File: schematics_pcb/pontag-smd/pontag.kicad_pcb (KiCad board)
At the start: 2 copper layers, 31 parts, among them J1 External 5V, J2 External 12V, J3 RS232 Port, J4 PS/2 Mouse, J5 AVR-ISP-6, J7 Extra, SW1 Reset, U1 LP2985-5.0, U3 ATmega8A-AU, U4 MAX232A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

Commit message: Update schematics and PCB
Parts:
- moved D5 120.9 mm to (72.4, 132.1), turned to 90 degrees
- moved R2 108.3 mm to (72.4, 138.4), turned to 270 degrees
- moved J7 97.1 mm to (95.2, 138.4), turned to 180 degrees
- moved JP1 75.6 mm to (115.6, 100.3)
- moved J5 64.8 mm to (95.2, 114.3)
- moved U4 39.9 mm to (83.8, 119.4)
- moved SW1 30.5 mm to (67.3, 134.6), turned to 90 degrees
- moved J4 15.3 mm to (85.1, 134.6), turned to 0 degrees
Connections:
- net Net-(C12-Pad1) renamed /REG_5V

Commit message: Changed some connectors
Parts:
- J5: value AVR-ISP-6 -> ISP; footprint Connector_PinHeader_2.54mm:PinHeader_2x03_P2.54mm_Vertical -> Connector_PinHeader_2.54mm:PinHeader_1x06_P2.54mm_Vertical
- J7: footprint Connector_PinSocket_2.54mm:PinSocket_2x06_P2.54mm_Vertical -> Connector_PinSocket_2.54mm:PinSocket_2x03_P2.54mm_Vertical
- moved J5 25.0 mm to (105.4, 137.2)
- moved J7 17.4 mm to (112.6, 137.2), turned to 0 degrees
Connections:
- SW1 pad 1: GND -> /RESET
- SW1 pad 2: /RESET -> GND
- U3 pad 26: Net-(J7-Pad7) -> (no net)
- U3 pad 27: Net-(J7-Pad9) -> (no net)
- U3 pad 28: Net-(J7-Pad11) -> (no net)

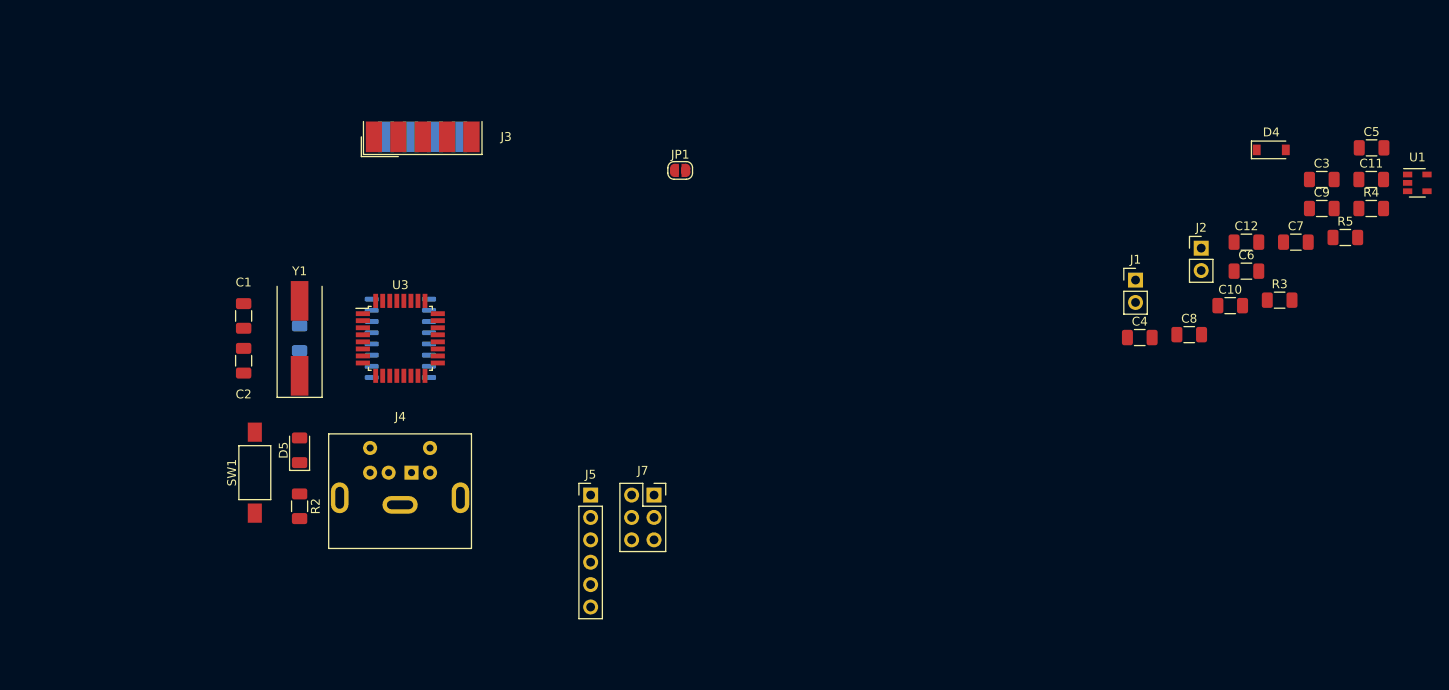
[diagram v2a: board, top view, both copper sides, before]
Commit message: Organize some components
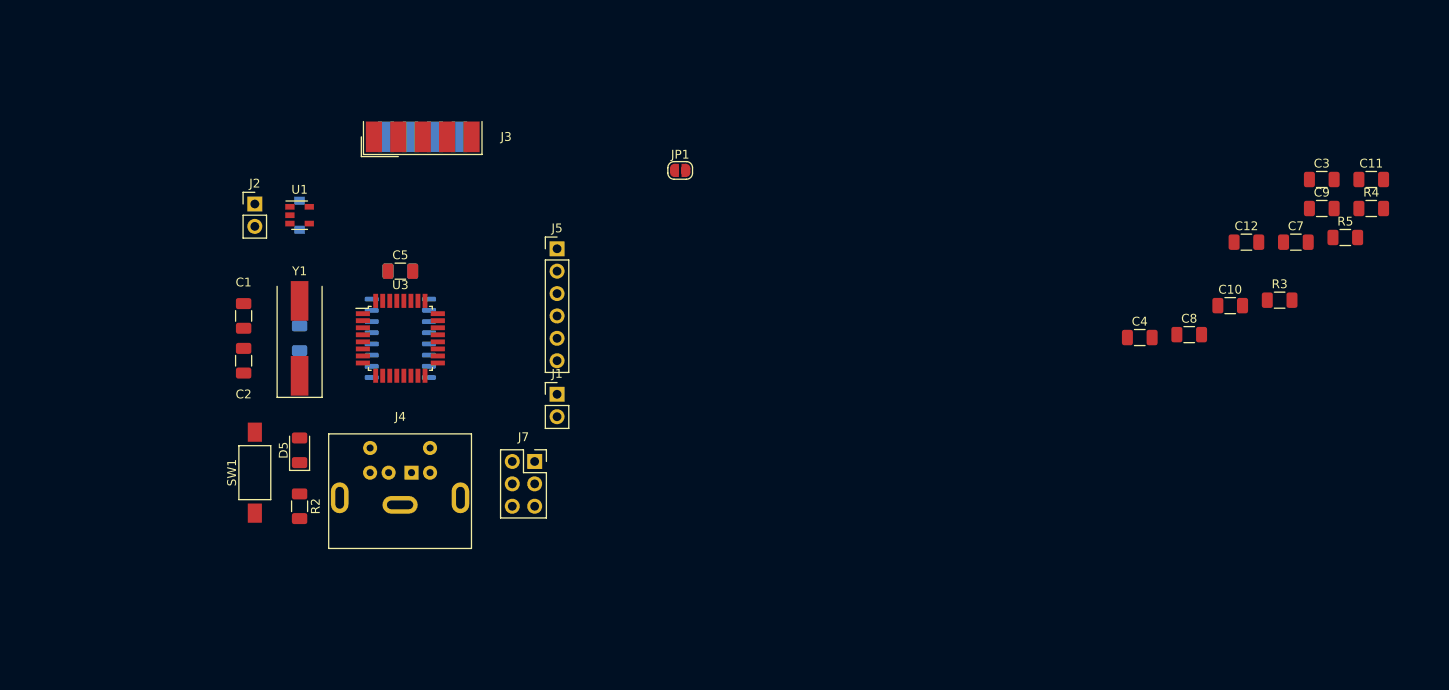
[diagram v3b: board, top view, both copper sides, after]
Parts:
- C6, D4: moved to B.Cu
- moved U1 126.9 mm to (72.4, 105.4)
- moved C5 111.1 mm to (83.8, 111.8)
- moved D4 110.5 mm to (72.4, 105.4), turned to 90 degrees
- moved J2 107.5 mm to (67.3, 104.1)
- moved C6 96.0 mm to (83.8, 111.8)
- moved J1 66.9 mm to (101.6, 125.7)
- moved J5 28.2 mm to (101.6, 109.2)
- moved J7 14.1 mm to (99.1, 133.3)

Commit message: Go on with board routing
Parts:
- C10, C11, C3, C7, C8, C9, R2, R3, R4, R5: moved to B.Cu
- J5: value ISP -> AVR-ISP-6; footprint Connector_PinHeader_2.54mm:PinHeader_1x06_P2.54mm_Vertical -> Connector_PinHeader_2.54mm:PinHeader_2x03_P2.54mm_Vertical
- moved R5 126.3 mm to (67.3, 133.3), turned to 270 degrees
- moved C3 116.2 mm to (72.4, 108.0)
- moved C11 115.5 mm to (78.7, 109.2)
- moved C9 111.3 mm to (77.5, 114.3), turned to 90 degrees
- moved R3 110.0 mm to (74.9, 132.1), turned to 90 degrees
- moved C12 107.4 mm to (72.4, 108.0), turned to 180 degrees
- moved R4 107.4 mm to (90.2, 132.1), turned to 270 degrees
- moved C7 106.8 mm to (78.7, 104.1), turned to 180 degrees
- moved C4 101.0 mm to (67.3, 108.0)
- moved C8 95.9 mm to (77.5, 120.7), turned to 90 degrees
- moved C10 95.8 mm to (82.5, 124.5)
- moved JP1 37.0 mm to (78.7, 104.1)
- moved R2 24.3 mm to (96.5, 135.9)
- moved D5 24.2 mm to (96.5, 133.3)
- moved J1 14.8 mm to (94.0, 113.0), turned to 90 degrees
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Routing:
- net /XTAL1: track 0.00 -> 10.0 mm
- net /XTAL2: track 0.00 -> 6.51 mm
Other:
- board outline added: 36.8 x 44.5 mm

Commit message: Updates on SMD PCB
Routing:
- net GND: track 0.00 -> 210.0 mm
- net VCC: track 0.00 -> 141.2 mm, vias 0 -> 2
- net /RESET: track 0.00 -> 100.7 mm, vias 0 -> 1
- net /MISO: track 0.00 -> 50.4 mm, vias 0 -> 1
- net /MOSI: track 0.00 -> 48.9 mm
- net /SCK: track 0.00 -> 43.3 mm
- net /RS232-RTS: track 0.00 -> 41.4 mm
- net /PS2-CLOCK: track 0.00 -> 29.9 mm, vias 0 -> 1
- net /PS2-DATA: track 0.00 -> 25.8 mm, vias 0 -> 1
- net /RS232-RX: track 0.00 -> 15.6 mm, vias 0 -> 1
- net Net-(C4-Pad1): track 0.00 -> 14.4 mm
- net /RS232-TX: track 0.00 -> 13.6 mm, vias 0 -> 1
- net +12V: track 0.00 -> 12.4 mm, vias 0 -> 1
- net /TTL-CTS: track 0.00 -> 12.0 mm, vias 0 -> 1
- net Net-(J7-Pad1): track 0.00 -> 11.9 mm
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- added copper zone on B.Cu, net GND
- added copper zone on F.Cu, net GND

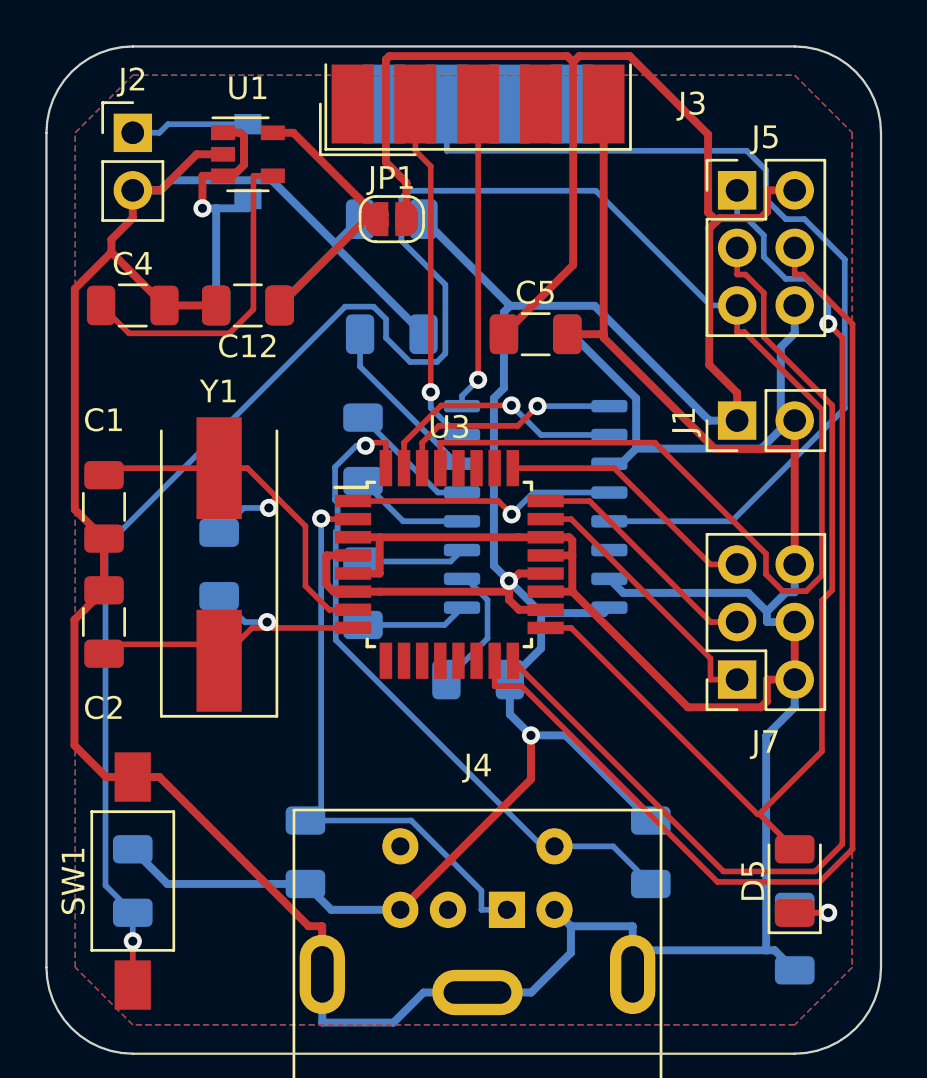
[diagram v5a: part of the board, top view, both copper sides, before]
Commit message: Add silkscreen text
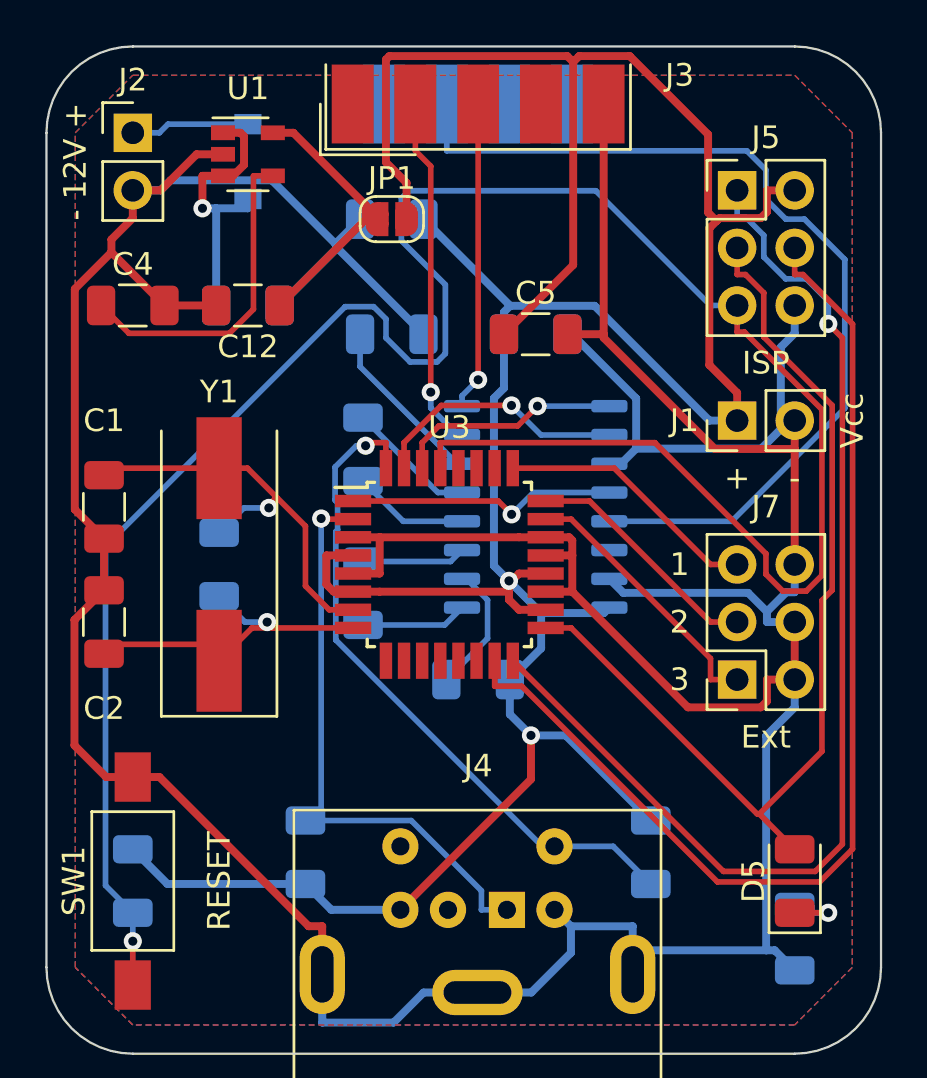
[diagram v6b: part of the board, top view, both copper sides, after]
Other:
- board text added: "+"
- board text added: "-"
- board text added: "- 12V +"
- board text added: "1"
- board text added: "2"
- board text added: "3"
- board text added: "Ext"
- board text added: "ISP"
- board text added: "PONTAG PS/2 -> Serial"
- board text added: "RESET"
- board text added: "Vcc"
- board text added: "v1.0"
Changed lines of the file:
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@@
   (general
     (thickness 1.6)
-    (drawings 8)
+    (drawings 20)
     (tracks 362)
     (zones 0)
@@
   (page A4)
   (layers
-    (0 F.Cu signal)
-    (31 B.Cu signal)
+    (0 F.Cu signal hide)
+    (31 B.Cu signal hide)
     (32 B.Adhes user)
     (33 F.Adhes user)
@@
     (descr "Through hole straight socket strip, 2x03, 2.54mm pitch, double cols (from Kicad 4.0.7), script generated")
     (tags "Through hole socket strip THT 2x03 2.54mm double row")
-    (fp_text reference J7 (at -1.27 -2.77) (layer F.SilkS)
+    (fp_text reference J7 (at -1.27 7.62) (layer F.SilkS)
       (effects (font (size 1 1) (thickness 0.15)))
     )
@@
     (tags "9-pin D-Sub connector edge mount solder cup female x-pin-pitch 2.77mm mounting holes distance 25mm")
     (attr smd)
-    (fp_text reference J3 (at -9.463333 0) (layer F.SilkS)
+    (fp_text reference J3 (at -8.89 1.27) (layer F.SilkS)
       (effects (font (size 1 1) (thickness 0.15)))
     )
@@
     (descr "Through hole straight pin header, 1x02, 2.54mm pitch, single row")
     (tags "Through hole pin header THT 1x02 2.54mm single row")
-    (fp_text reference J1 (at 0 -2.33 90) (layer F.SilkS)
+    (fp_text reference J1 (at 0 -2.33) (layer F.SilkS)
       (effects (font (size 1 1) (thickness 0.15)))
     )
@@
     )
   )
+  (gr_text v1.0 (at 69.85 138.43) (layer B.SilkS)
+    (effects (font (size 1 1) (thickness 0.15)) (justify mirror))
+  )
+  (gr_text "PONTAG\nPS/2 -> Serial" (at 73.66 127) (layer B.SilkS)
+    (effects (font (size 1 1) (thickness 0.15)) (justify mirror))
+  )
+  (gr_text Vcc (at 99.06 113.03 90) (layer F.SilkS)
+    (effects (font (size 1 1) (thickness 0.15)))
+  )
+  (gr_text - (at 96.52 115.57) (layer F.SilkS)
+    (effects (font (size 1 1) (thickness 0.15)))
+  )
+  (gr_text + (at 93.98 115.57) (layer F.SilkS)
+    (effects (font (size 1 1) (thickness 0.15)))
+  )
+  (gr_text ISP (at 95.25 110.49) (layer F.SilkS)
+    (effects (font (size 1 1) (thickness 0.15)))
+  )
+  (gr_text Ext (at 95.25 127) (layer F.SilkS)
+    (effects (font (size 1 1) (thickness 0.15)))
+  )
+  (gr_text 3 (at 91.44 124.46) (layer F.SilkS)
+    (effects (font (size 1 1) (thickness 0.15)))
+  )
+  (gr_text 2 (at 91.44 121.92) (layer F.SilkS)
+    (effects (font (size 1 1) (thickness 0.15)))
+  )
+  (gr_text 1 (at 91.44 119.38) (layer F.SilkS)
+    (effects (font (size 1 1) (thickness 0.15)))
+  )
+  (gr_text RESET (at 71.12 133.35 90) (layer F.SilkS)
+    (effects (font (size 1 1) (thickness 0.15)))
+  )
+  (gr_text "- 12V +" (at 64.77 101.6 90) (layer F.SilkS)
+    (effects (font (size 1 1) (thickness 0.15)))
+  )
   (gr_arc (start 67.31 137.16) (end 63.5 137.16) (angle -90) (layer Edge.Cuts) (width 0.1))

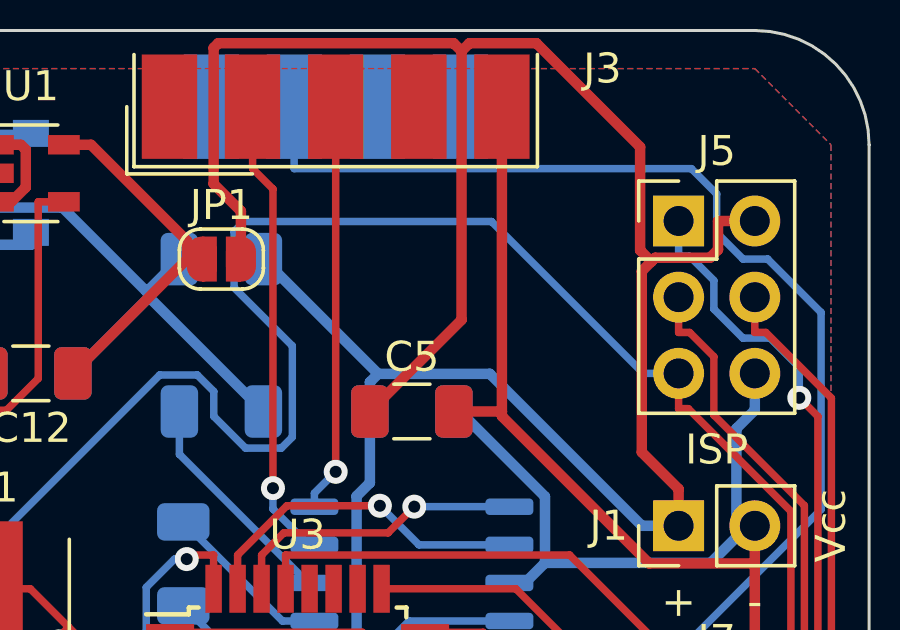
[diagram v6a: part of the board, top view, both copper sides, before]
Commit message: Add logo to board
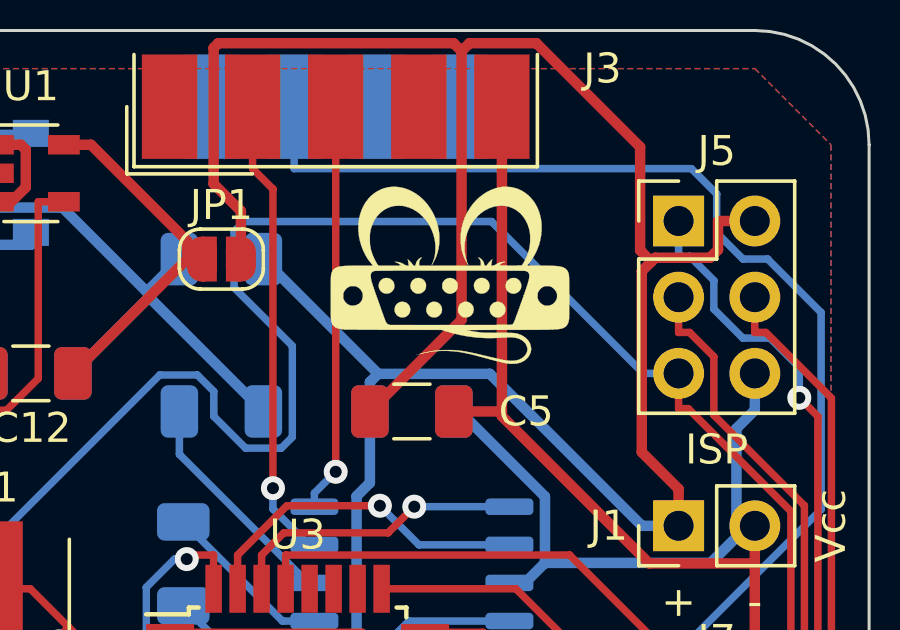
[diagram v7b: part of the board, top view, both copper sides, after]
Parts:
- added G***: LOGO, extra:logo, F.Cu at (86.4, 104.7)

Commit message: Minimal changes to silkscreen
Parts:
- J1: value External 5V -> Ext. VCC
- J7: footprint Connector_PinSocket_2.54mm:PinSocket_2x03_P2.54mm_Vertical -> Connector_PinHeader_2.54mm:PinHeader_2x03_P2.54mm_Vertical
- moved J7 5.08 mm to (94.0, 119.4), turned to 0 degrees
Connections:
- U3 pad 23: Net-(J7-Pad1) -> Net-(J7-Pad5)
- U3 pad 25: Net-(J7-Pad5) -> Net-(J7-Pad1)
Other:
- board text added: "v1.1"
- board text removed: "Ext"
- board text removed: "ISP"
- board text removed: "RESET"
- board text removed: "Vcc"
- board text removed: "v1.0"
